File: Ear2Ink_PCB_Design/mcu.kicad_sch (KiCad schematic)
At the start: 32 parts, among them J1 Conn_02x16_Top_Bottom, J2 Conn_01x08_Pin, J3 Conn_01x08_Pin, J4 Micro_SD_Card_Det1, J5 Conn_01x06_Pin, SW1 SW_Push, U1 STM32F411RETx, Y1 MAX7375AXR805

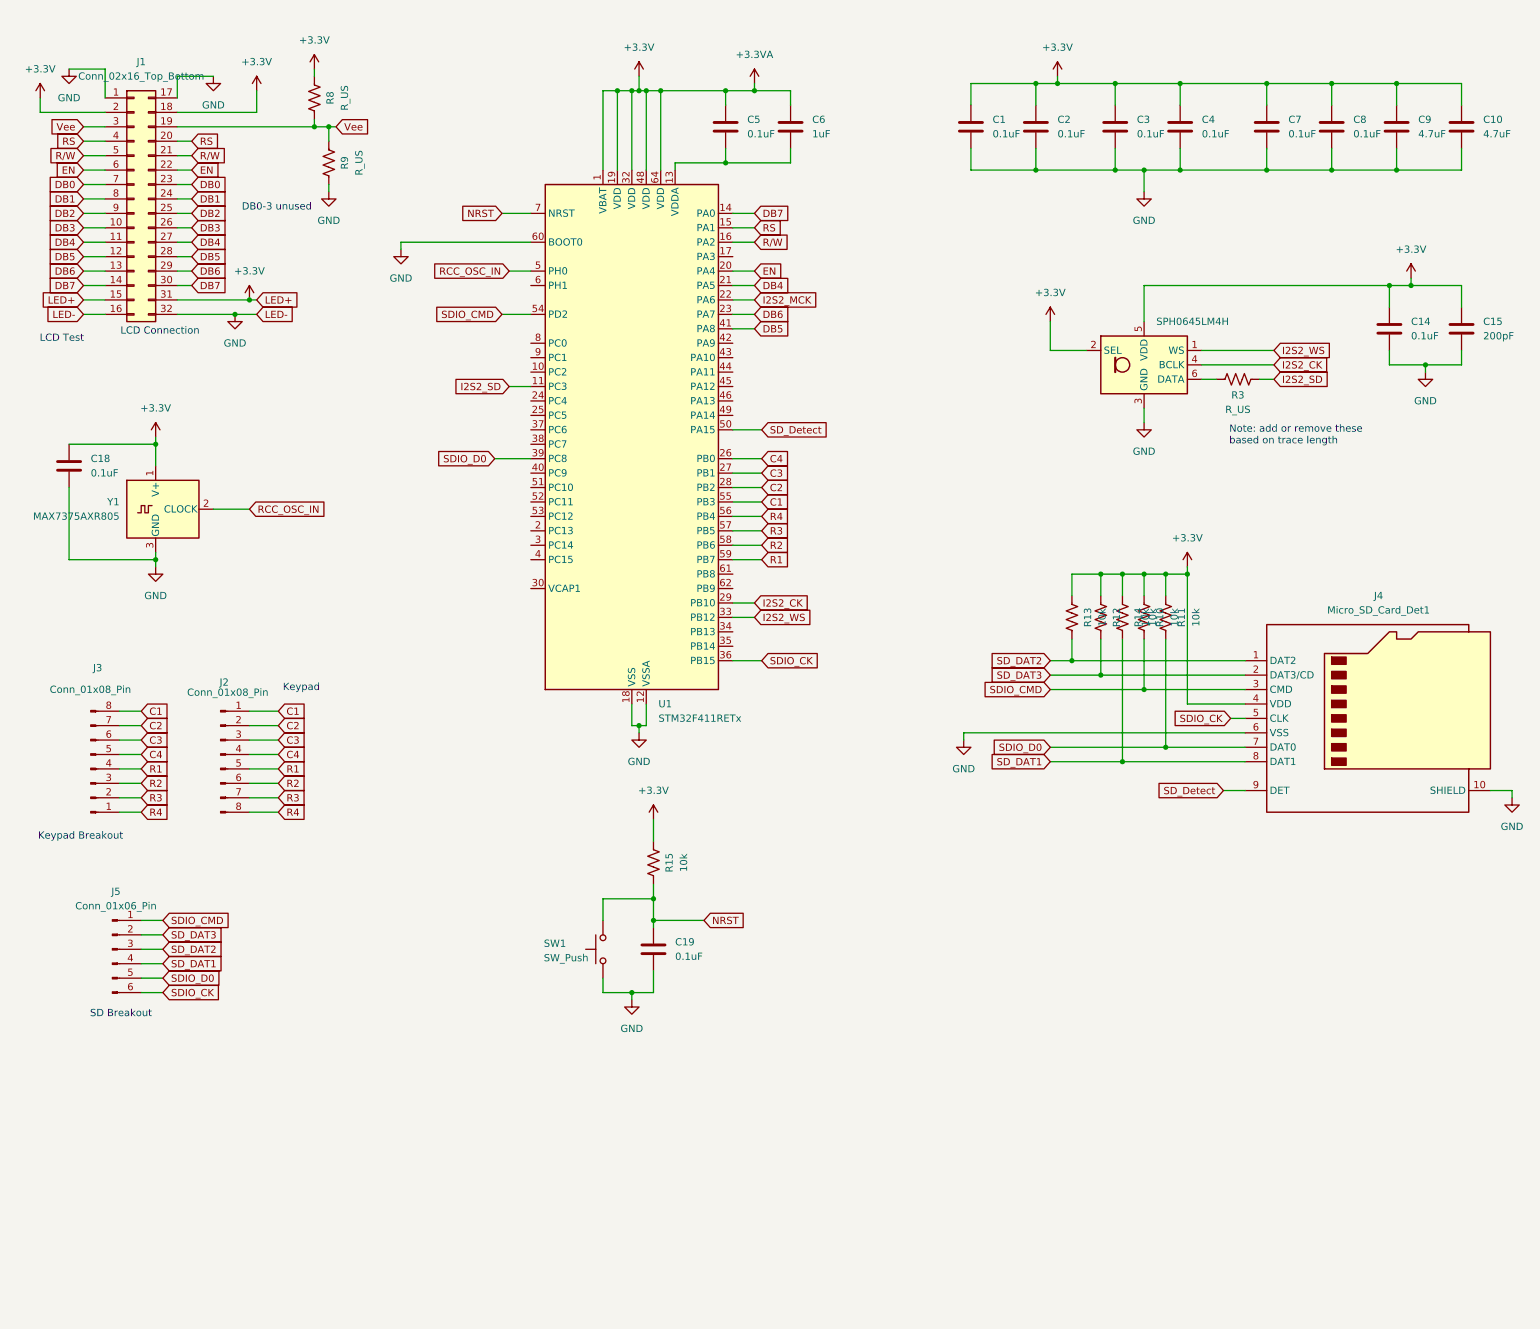
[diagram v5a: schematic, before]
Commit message: added esd prot and programming header
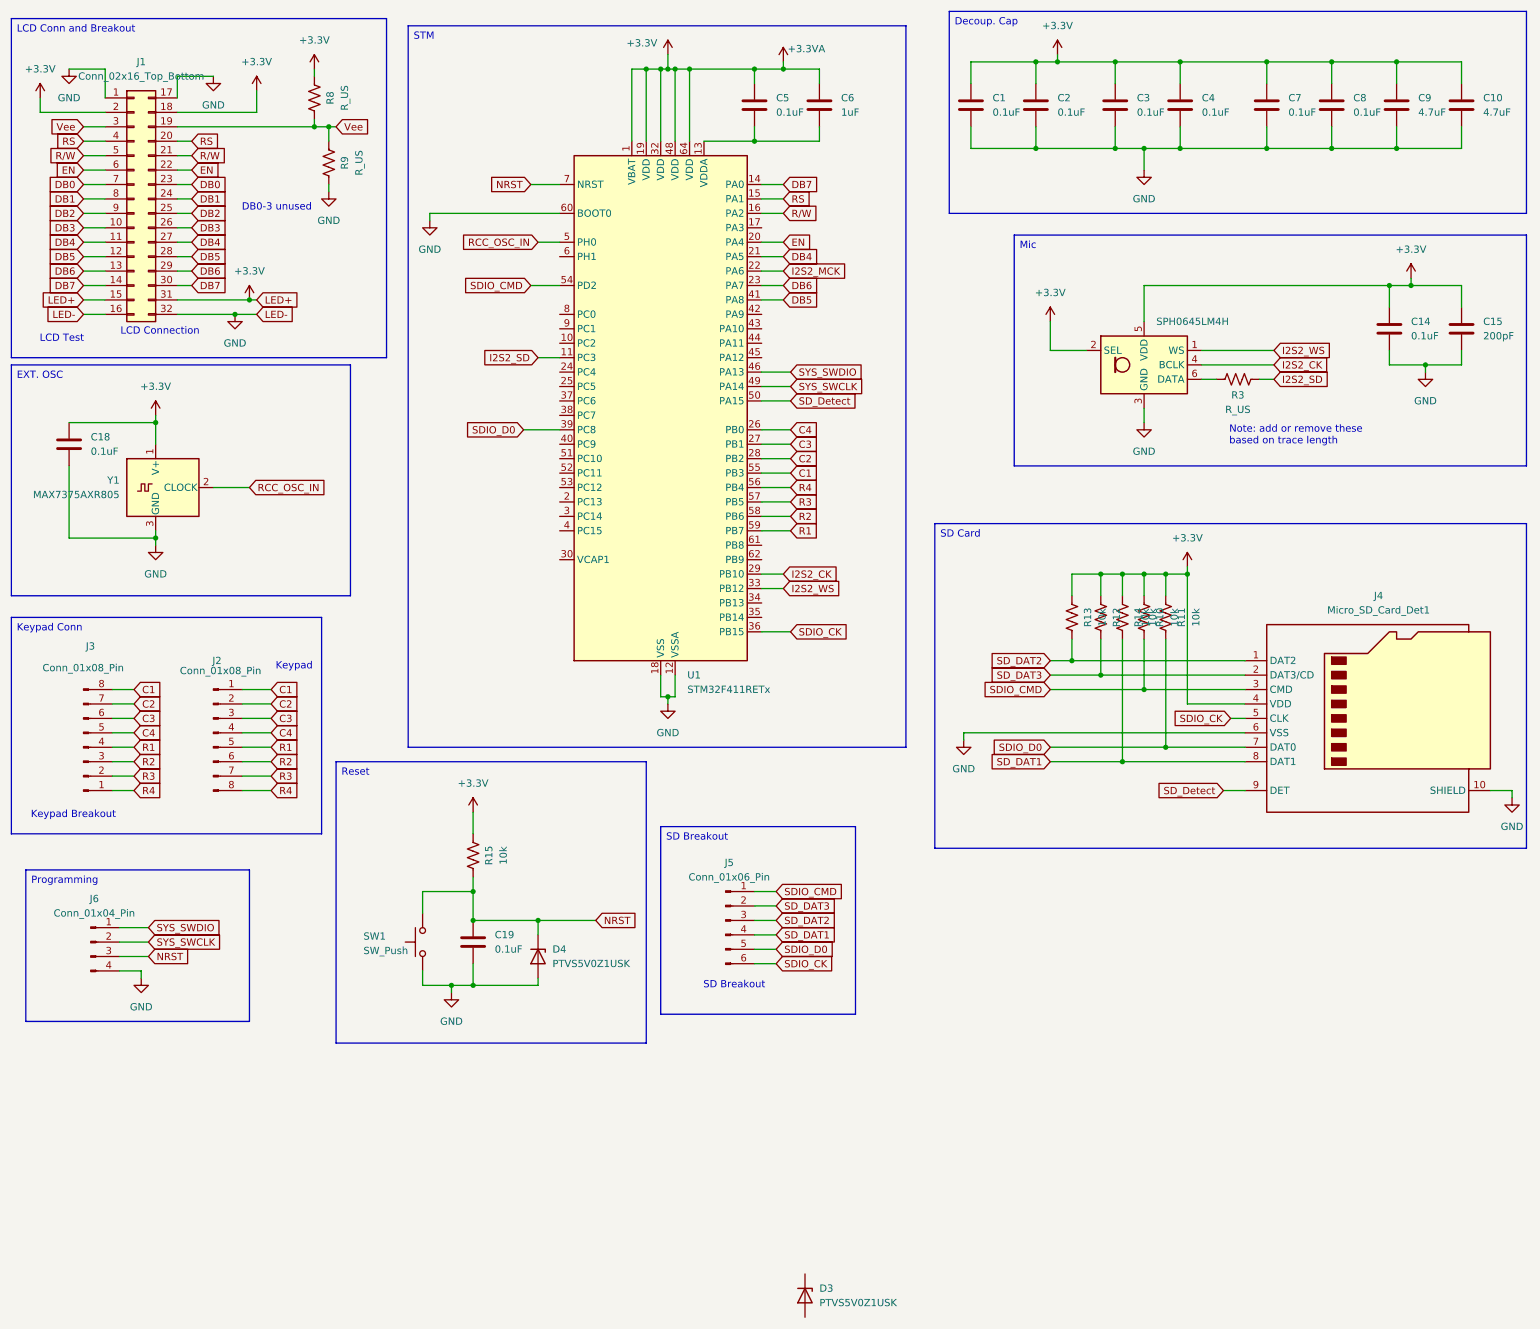
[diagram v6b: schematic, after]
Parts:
- added D3, D4: PTVS5V0Z1USK, Diode_SMD:Nexperia_DSN1608-2_1.6x0.8mm, symbol Diode:PTVS5V0Z1USK
- added J6: Conn_01x04_Pin, symbol Connector:Conn_01x04_Pin
- C1, C10, C2, C3, C4, C5, C7, C8, C9: footprint (none) -> Capacitor_SMD:C_0603_1608Metric_Pad1.08x0.95mm_HandSolder
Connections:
- net GND: now also D4.2 (A), J6.4 (Pin_4)
- net NRST: now also D4.1 (K), J6.3 (Pin_3)
- net SYS_SWDIO: now reaches U1.46 (PA13)
- net SYS_SWDIO: now also J6.1 (Pin_1)
- net SYS_SWCLK: now reaches U1.49 (PA14)
- net SYS_SWCLK: now also J6.2 (Pin_2)
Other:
- moved on the sheet: C1, C10, C18, C19, C2, C3, C4, C5, C6, C7, C8, C9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

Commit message: footprints
missing L tho
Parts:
- C14, C18, C19, C6: footprint (none) -> Capacitor_SMD:C_0603_1608Metric_Pad1.08x0.95mm_HandSolder
- C15: footprint (none) -> Capacitor_SMD:C_0805_2012Metric_Pad1.18x1.45mm_HandSolder
- J1: footprint (none) -> Connector_PinHeader_2.54mm:PinHeader_2x16_P2.54mm_Vertical
- J2, J3: footprint (none) -> Connector_PinHeader_2.54mm:PinHeader_1x08_P2.54mm_Vertical
- J4: footprint (none) -> Connector_Card:SD-SIM_microSD-microSIM_Molex_104168-1620
- J5: footprint (none) -> Connector_PinHeader_2.54mm:PinHeader_1x06_P2.54mm_Vertical
- J6: footprint (none) -> Connector_PinHeader_2.54mm:PinHeader_1x04_P2.54mm_Vertical
- SW1: footprint (none) -> Button:SW_FSM2JMTR_TEC
- U1: footprint LQFP64-10x10mm -> STM:LQFP64-10x10mm
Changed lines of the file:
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@@
 			)
 		)
-		(property "Footprint" ""
+		(property "Footprint" "Connector_PinHeader_2.54mm:PinHeader_1x04_P2.54mm_Vertical"
 			(at 30.48 177.8 0)
 			(effects
@@
 			)
 		)
-		(property "Footprint" "LQFP64-10x10mm"
+		(property "Footprint" "STM:LQFP64-10x10mm"
 			(at 115.57 128.27 0)
 			(effects
@@
 			)
 		)
-		(property "Footprint" ""
+		(property "Footprint" "Button:SW_FSM2JMTR_TEC"
 			(at 83.82 177.8 0)
 			(effects
@@
 			)
 		)
-		(property "Footprint" ""
+		(property "Footprint" "Capacitor_SMD:C_0603_1608Metric_Pad1.08x0.95mm_HandSolder"
 			(at 27.6352 93.98 0)
 			(effects
@@
 			)
 		)
-		(property "Footprint" ""
+		(property "Footprint" "Capacitor_SMD:C_0603_1608Metric_Pad1.08x0.95mm_HandSolder"
 			(at 260.0452 73.66 0)
 			(effects
@@
 			)
 		)
-		(property "Footprint" ""
+		(property "Footprint" "Connector_PinHeader_2.54mm:PinHeader_1x08_P2.54mm_Vertical"
 			(at 52.07 140.97 0)
 			(effects
@@
 			)
 		)
-		(property "Footprint" ""
+		(property "Footprint" "Connector_PinHeader_2.54mm:PinHeader_2x16_P2.54mm_Vertical"
 			(at 38.1 46.99 0)
 			(effects
@@
 			)
 		)
-		(property "Footprint" ""
+		(property "Footprint" "Capacitor_SMD:C_0603_1608Metric_Pad1.08x0.95mm_HandSolder"
 			(at 98.7552 181.61 0)
 			(effects
@@
 			)
 		)
-		(property "Footprint" ""
+		(property "Footprint" "Capacitor_SMD:C_0603_1608Metric_Pad1.08x0.95mm_HandSolder"
 			(at 159.7152 34.29 0)
 			(effects
@@
 			)
 		)
-		(property "Footprint" ""
+		(property "Footprint" "Connector_PinHeader_2.54mm:PinHeader_1x08_P2.54mm_Vertical"
 			(at 29.21 143.51 0)
 			(effects
@@
 			)
 		)
-		(property "Footprint" ""
+		(property "Footprint" "Capacitor_SMD:C_0805_2012Metric_Pad1.18x1.45mm_HandSolder"
 			(at 272.7452 73.66 0)
 			(effects
@@
 			)
 		)
-		(property "Footprint" ""
+		(property "Footprint" "Connector_Card:SD-SIM_microSD-microSIM_Molex_104168-1620"
 			(at 308.61 120.65 0)
 			(effects
@@
 			)
 		)
-		(property "Footprint" ""
+		(property "Footprint" "Connector_PinHeader_2.54mm:PinHeader_1x06_P2.54mm_Vertical"
 			(at 142.24 173.99 0)
 			(effects

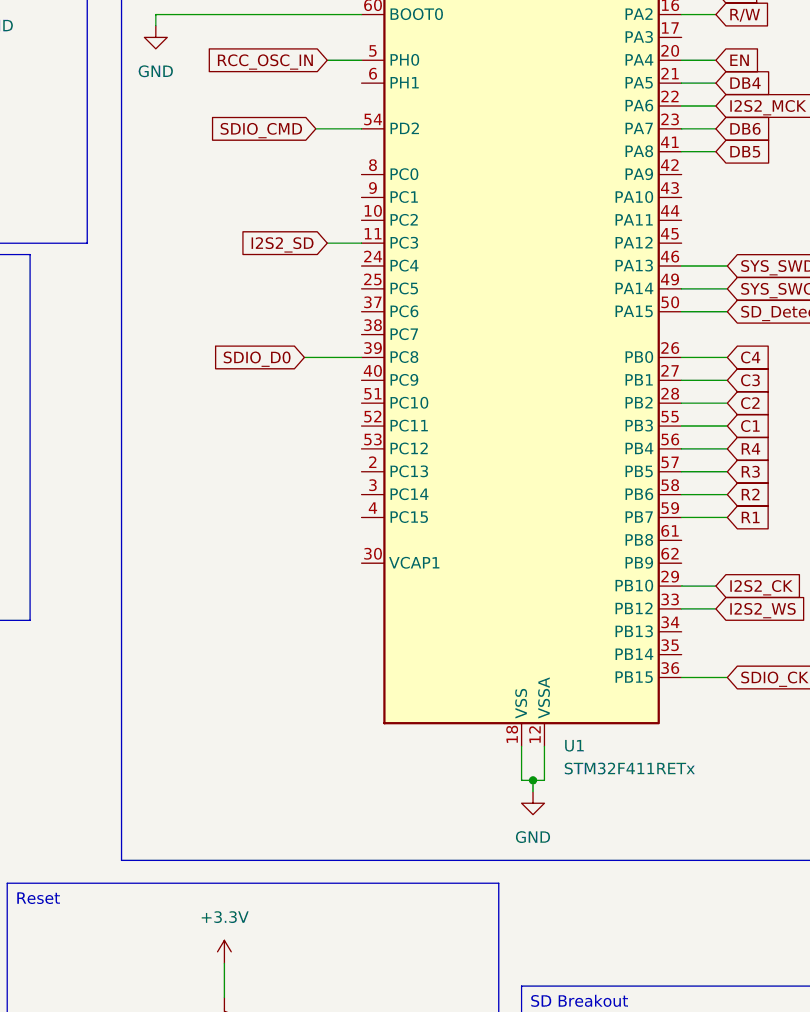
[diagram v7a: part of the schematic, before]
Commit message: added current monitor
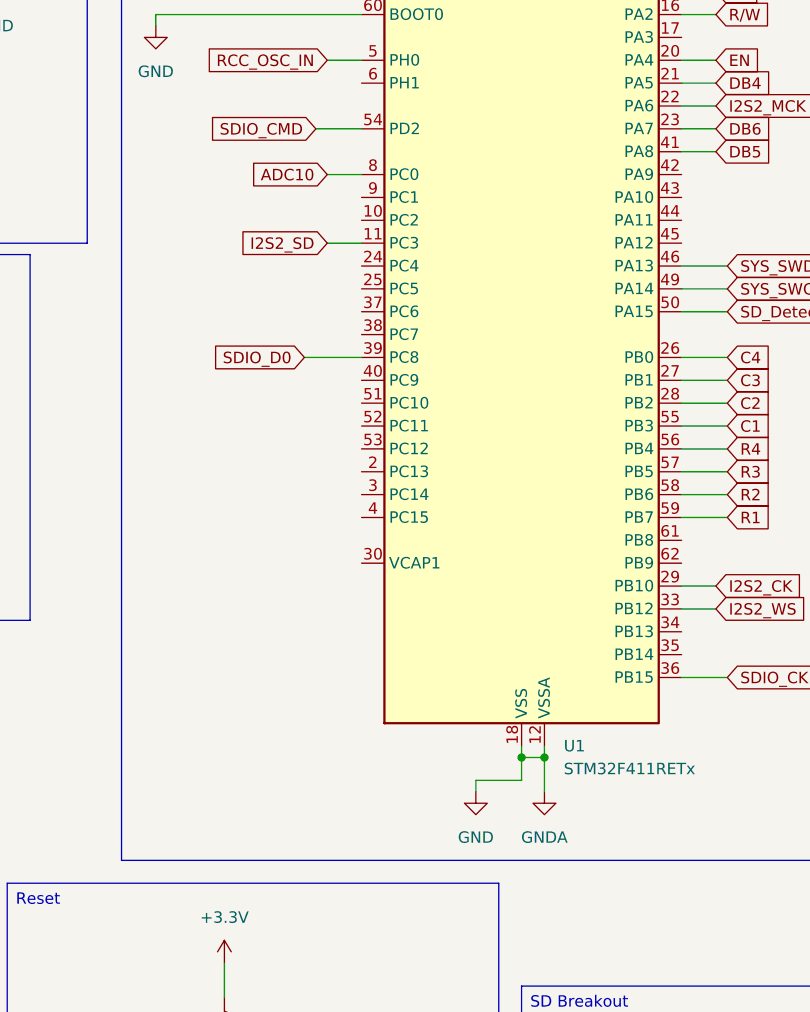
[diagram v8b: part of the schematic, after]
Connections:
- net ADC10: now reaches U1.8 (PC0)
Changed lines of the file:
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@@
 	)
 	(junction
+		(at 133.35 132.08)
+		(diameter 0)
+		(color 0 0 0 0)
+	)
+	(junction
 		(at 196.85 22.86)
 		(diameter 0)
@@
 	)
 	(junction
-		(at 223.52 113.03)
+		(at 130.81 132.08)
 		(diameter 0)
 		(color 0 0 0 0)
 	)
 	(junction
-		(at 72.39 34.29)
+		(at 223.52 113.03)
 		(diameter 0)
 		(color 0 0 0 0)
 	)
 	(junction
-		(at 200.66 22.86)
+		(at 72.39 34.29)
 		(diameter 0)
 		(color 0 0 0 0)
 	)
 	(junction
-		(at 248.92 38.1)
+		(at 200.66 22.86)
 		(diameter 0)
 		(color 0 0 0 0)
 	)
 	(junction
-		(at 132.08 134.62)
+		(at 248.92 38.1)
 		(diameter 0)
 		(color 0 0 0 0)
@@
 	)
 	(junction
-		(at 135.89 24.13)
-		(diameter 0)
-		(color 0 0 0 0)
-	)
-	(junction
 		(at 260.35 38.1)
 		(diameter 0)
@@
 	)
 	(junction
-		(at 147.32 24.13)
-		(diameter 0)
-		(color 0 0 0 0)
-	)
-	(junction
 		(at 97.79 173.99)
 		(diameter 0)
@@
 	)
 	(junction
+		(at 135.89 24.13)
+		(diameter 0)
+		(color 0 0 0 0)
+	)
+	(junction
 		(at 208.28 130.81)
 		(diameter 0)
@@
 	)
 	(junction
+		(at 147.32 24.13)
+		(diameter 0)
+		(color 0 0 0 0)
+	)
+	(junction
 		(at 208.28 113.03)
 		(diameter 0)
@@
 	(wire
 		(pts
+			(xy 130.81 132.08) (xy 130.81 130.81)
+		)
+		(stroke
+			(width 0)
+			(type default)
+		)
+	)
+	(wire
+		(pts
 			(xy 203.2 128.27) (xy 233.68 128.27)
 		)
@@
 	(wire
 		(pts
+			(xy 133.35 132.08) (xy 133.35 135.89)
+		)
+		(stroke
+			(width 0)
+			(type default)
+		)
+	)
+	(wire
+		(pts
+			(xy 130.81 132.08) (xy 133.35 132.08)
+		)
+		(stroke
+			(width 0)
+			(type default)
+		)
+	)
+	(wire
+		(pts
 			(xy 208.28 113.03) (xy 208.28 116.84)
 		)
@@
 	(wire
 		(pts
+			(xy 130.81 134.62) (xy 130.81 132.08)
+		)
+		(stroke
+			(width 0)
+			(type default)
+		)
+	)
+	(wire
+		(pts
 			(xy 69.85 24.13) (xy 69.85 25.4)
 		)
@@
 	(wire
 		(pts
-			(xy 133.35 134.62) (xy 133.35 130.81)
-		)
-		(stroke
-			(width 0)
-			(type default)
-		)
-	)
-	(wire
-		(pts
 			(xy 237.49 38.1) (xy 248.92 38.1)
 		)
@@
 	(wire
 		(pts
-			(xy 135.89 24.13) (xy 147.32 24.13)
+			(xy 158.75 24.13) (xy 158.75 26.67)
 		)
 		(stroke
@@
 	(wire
 		(pts
-			(xy 158.75 24.13) (xy 158.75 26.67)
+			(xy 248.92 22.86) (xy 248.92 26.67)
 		)
 		(stroke
@@
 	(wire
 		(pts
-			(xy 248.92 22.86) (xy 248.92 26.67)
+			(xy 271.78 34.29) (xy 271.78 38.1)
 		)
 		(stroke
@@
 	(wire
 		(pts
-			(xy 271.78 34.29) (xy 271.78 38.1)
+			(xy 147.32 36.83) (xy 158.75 36.83)
 		)
 		(stroke
@@
 	(wire
 		(pts
-			(xy 147.32 36.83) (xy 158.75 36.83)
+			(xy 222.25 22.86) (xy 237.49 22.86)
 		)
 		(stroke
@@
 	(wire
 		(pts
-			(xy 222.25 22.86) (xy 237.49 22.86)
+			(xy 29.21 49.53) (xy 33.02 49.53)
 		)
 		(stroke
@@
 	(wire
 		(pts
-			(xy 29.21 49.53) (xy 33.02 49.53)
+			(xy 148.59 54.61) (xy 152.4 54.61)
 		)
 		(stroke
@@
 	(wire
 		(pts
-			(xy 148.59 54.61) (xy 152.4 54.61)
+			(xy 135.89 24.13) (xy 147.32 24.13)
 		)
 		(stroke
@@
 	(wire
 		(pts
-			(xy 130.81 130.81) (xy 130.81 134.62)
-		)
-		(stroke
-			(width 0)
-			(type default)
-		)
-	)
-	(wire
-		(pts
 			(xy 109.22 74.93) (xy 113.03 74.93)
 		)
@@
 	(wire
 		(pts
-			(xy 130.81 134.62) (xy 132.08 134.62)
-		)
-		(stroke
-			(width 0)
-			(type default)
-		)
-	)
-	(wire
-		(pts
 			(xy 35.56 175.26) (xy 40.64 175.26)
 		)
@@
 	(wire
 		(pts
+			(xy 133.35 130.81) (xy 133.35 132.08)
+		)
+		(stroke
+			(width 0)
+			(type default)
+		)
+	)
+	(wire
+		(pts
 			(xy 106.68 87.63) (xy 113.03 87.63)
 		)
@@
 	(wire
 		(pts
-			(xy 132.08 134.62) (xy 132.08 135.89)
+			(xy 125.73 134.62) (xy 125.73 135.89)
 		)
 		(stroke
@@
 	(wire
 		(pts
-			(xy 41.91 105.41) (xy 41.91 106.68)
+			(xy 109.22 67.31) (xy 113.03 67.31)
 		)
 		(stroke
@@
 	(wire
 		(pts
-			(xy 148.59 123.19) (xy 153.67 123.19)
+			(xy 41.91 105.41) (xy 41.91 106.68)
 		)
 		(stroke
@@
 	(wire
 		(pts
-			(xy 109.22 184.15) (xy 109.22 185.42)
+			(xy 148.59 123.19) (xy 153.67 123.19)
 		)
 		(stroke
@@
 	(wire
 		(pts
-			(xy 132.08 134.62) (xy 133.35 134.62)
+			(xy 109.22 184.15) (xy 109.22 185.42)
 		)
 		(stroke
@@
 	(wire
 		(pts
+			(xy 125.73 134.62) (xy 130.81 134.62)
+		)
+		(stroke
+			(width 0)
+			(type default)
+		)
+	)
+	(wire
+		(pts
 			(xy 223.52 111.76) (xy 223.52 113.03)
 		)
@@
 		)
 	)
+	(global_label "ADC10"
+		(shape input)
+		(at 109.22 67.31 180)
+		(fields_autoplaced yes)
+		(effects
+			(font
+				(size 1.27 1.27)
+			)
+			(justify right)
+		)
+		(property "Intersheetrefs" "${INTERSHEET_REFS}"
+			(at 100.1872 67.31 0)
+			(effects
+				(font
+					(size 1.27 1.27)
+				)
+				(justify right)
+				(hide yes)
+			)
+		)
+	)
 	(global_label "DB2"
 		(shape input)
@@
 	(symbol
 		(lib_id "power:GND")
-		(at 132.08 135.89 0)
+		(at 125.73 135.89 0)
 		(unit 1)
 		(exclude_from_sim no)
@@
 		(fields_autoplaced yes)
 		(property "Reference" "#PWR04"
-			(at 132.08 142.24 0)
+			(at 125.73 142.24 0)
 			(effects
 				(font
@@
 		)
 		(property "Value" "GND"
-			(at 132.08 140.97 0)
+			(at 125.73 140.97 0)
 			(effects
 				(font
@@
 		)
 		(property "Footprint" ""
-			(at 132.08 135.89 0)
+			(at 125.73 135.89 0)
 			(effects
 				(font
@@
 		)
 		(property "Datasheet" ""
-			(at 132.08 135.89 0)
+			(at 125.73 135.89 0)
 			(effects
 				(font
@@
 		)
 		(property "Description" "Power symbol creates a global label with name \"GND\" , ground"
-			(at 132.08 135.89 0)
+			(at 125.73 135.89 0)
 			(effects
 				(font
@@
 					(unit 1)
 				)
+			)
+		)
+	)
+	(symbol
+		(lib_id "power:GNDA")
+		(at 133.35 135.89 0)
+		(unit 1)
+		(exclude_from_sim no)
+		(in_bom yes)
+		(on_board yes)
+		(dnp no)
+		(fields_autoplaced yes)
+		(property "Reference" "#PWR037"
+			(at 133.35 142.24 0)
+			(effects
+				(font
+					(size 1.27 1.27)
+				)
+				(hide yes)
+			)
+		)
+		(property "Value" "GNDA"
+			(at 133.35 140.97 0)
+			(effects
+				(font
+					(size 1.27 1.27)
+				)
+			)
+		)
+		(property "Footprint" ""
+			(at 133.35 135.89 0)
+			(effects
+				(font
+					(size 1.27 1.27)
+				)
+				(hide yes)
+			)
+		)
+		(property "Datasheet" ""
+			(at 133.35 135.89 0)
+			(effects
+				(font
+					(size 1.27 1.27)
+				)
+				(hide yes)
+			)
+		)
+		(property "Description" "Power symbol creates a global label with name \"GNDA\" , analog ground"
+			(at 133.35 135.89 0)
+			(effects
+				(font
+					(size 1.27 1.27)
+				)
+				(hide yes)
+			)
+		)
+		(pin "1"
+		)
+		(instances
+			(project ""
+				(path "/cdb6d8ac-bdfd-4608-bf70-aa82e76498ad/2ddad00a-af62-4659-9017-a3cd158a818d"
+					(reference "#PWR037")
+					(unit 1)
+				)
